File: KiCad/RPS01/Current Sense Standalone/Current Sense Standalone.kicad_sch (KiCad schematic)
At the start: 4 parts, among them U1 INA139QPWRQ1

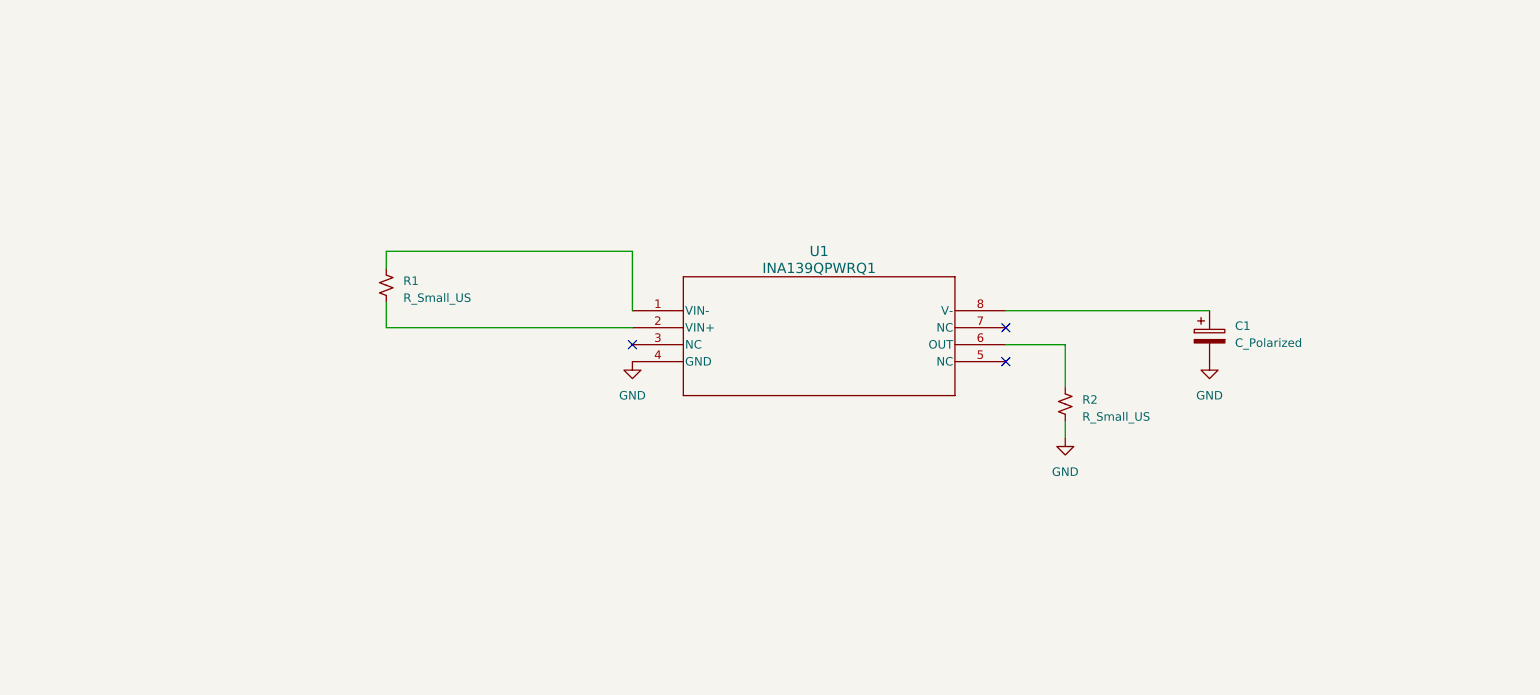
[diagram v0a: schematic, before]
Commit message: Current Sense
Updated schematic
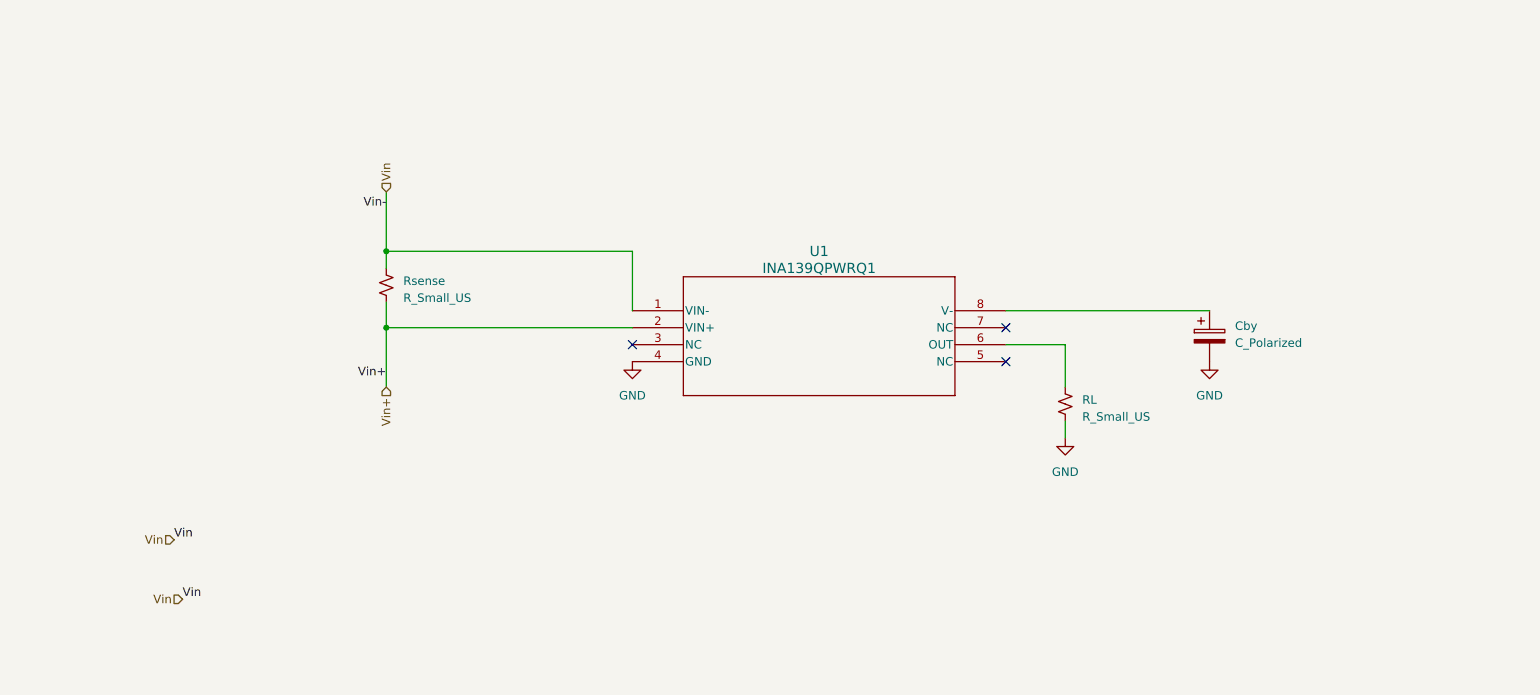
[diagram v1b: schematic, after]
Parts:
- renumbered C1 to Cby, R2 to RL, R1 to Rsense
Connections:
- net Vin: now reaches Rsense.1, U1.1 (VIN-)
- net Vin+: now reaches Rsense.2, U1.2 (VIN+)
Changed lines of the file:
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@@
 (kicad_sch (version 20230121) (generator eeschema)
   (paper "A4")
+  (junction (at 86.36 88.9) (diameter 0) (color 0 0 0 0)
+  )
+  (junction (at 86.36 100.33) (diameter 0) (color 0 0 0 0)
+  )
   (no_connect (at 123.19 102.87))
   (no_connect (at 179.07 100.33))
   (no_connect (at 179.07 105.41))
+  (wire (pts (xy 86.36 80.01) (xy 86.36 88.9))
+    (stroke (width 0) (type default))
+  )
+  (wire (pts (xy 86.36 100.33) (xy 86.36 109.22))
+    (stroke (width 0) (type default))
+  )
   (wire (pts (xy 86.36 88.9) (xy 86.36 91.44))
     (stroke (width 0) (type default))
@@
     (stroke (width 0) (type default))
   )
+  (label "Vin" (at 54.61 132.08 0) (fields_autoplaced)
+    (effects (font (size 1.27 1.27)) (justify left bottom))
+  )
+  (label "Vin+" (at 86.36 107.95 180) (fields_autoplaced)
+    (effects (font (size 1.27 1.27)) (justify right bottom))
+  )
+  (label "Vin" (at 55.88 140.97 0) (fields_autoplaced)
+    (effects (font (size 1.27 1.27)) (justify left bottom))
+  )
+  (label "Vin-" (at 86.36 82.55 180) (fields_autoplaced)
+    (effects (font (size 1.27 1.27)) (justify right bottom))
+  )
+  (hierarchical_label "Vin" (shape input) (at 55.88 140.97 180) (fields_autoplaced)
+    (effects (font (size 1.27 1.27)) (justify right))
+  )
+  (hierarchical_label "Vin" (shape input) (at 86.36 80.01 90) (fields_autoplaced)
+    (effects (font (size 1.27 1.27)) (justify left))
+  )
+  (hierarchical_label "Vin+" (shape input) (at 86.36 109.22 270) (fields_autoplaced)
+    (effects (font (size 1.27 1.27)) (justify right))
+  )
+  (hierarchical_label "Vin" (shape input) (at 54.61 132.08 180) (fields_autoplaced)
+    (effects (font (size 1.27 1.27)) (justify right))
+  )
   (symbol (lib_id "Device:R_Small_US") (at 187.96 111.76 0) (unit 1)
     (in_bom yes) (on_board yes) (dnp no) (fields_autoplaced)
-    (property "Reference" "R2" (at 190.5 111.125 0)
+    (property "Reference" "RL" (at 190.5 111.125 0)
       (effects (font (size 1.27 1.27)) (justify left))
     )
@@
       (project "Current Sense Standalone"
         (path "/af3dddb2-191c-40a1-9395-0fad50eefcf8"
-          (reference "R2") (unit 1)
+          (reference "RL") (unit 1)
         )
       )
@@
   (symbol (lib_id "Device:C_Polarized") (at 209.55 101.6 0) (unit 1)
     (in_bom yes) (on_board yes) (dnp no) (fields_autoplaced)
-    (property "Reference" "C1" (at 213.36 100.076 0)
+    (property "Reference" "Cby" (at 213.36 100.076 0)
       (effects (font (size 1.27 1.27)) (justify left))
     )
@@
       (project "Current Sense Standalone"
         (path "/af3dddb2-191c-40a1-9395-0fad50eefcf8"
-          (reference "C1") (unit 1)
+          (reference "Cby") (unit 1)
         )
       )
@@
   (symbol (lib_id "Device:R_Small_US") (at 86.36 93.98 0) (unit 1)
     (in_bom yes) (on_board yes) (dnp no) (fields_autoplaced)
-    (property "Reference" "R1" (at 88.9 93.345 0)
+    (property "Reference" "Rsense" (at 88.9 93.345 0)
       (effects (font (size 1.27 1.27)) (justify left))
     )
@@
       (project "Current Sense Standalone"
         (path "/af3dddb2-191c-40a1-9395-0fad50eefcf8"
-          (reference "R1") (unit 1)
-        )
-      )
+          (reference "Rsense") (unit 1)
+        )
+      )

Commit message: updated Current sense circuit
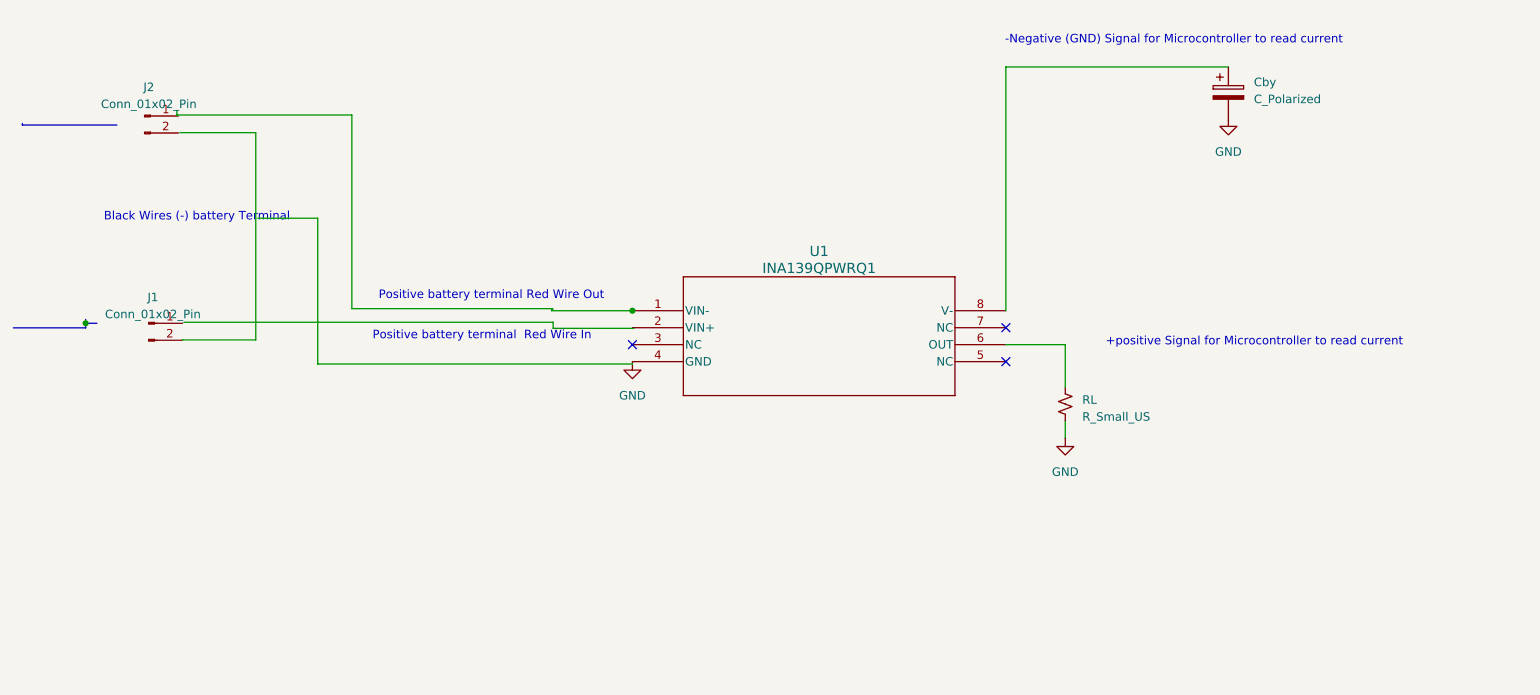
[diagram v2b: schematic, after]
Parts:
- removed Rsense: R_Small_US, Res_Bourns_CSS2H-3920R-L300F:Bourns-CSS2H-3920R-L300F-MFG, symbol Device:R_Small_US
- added J1, J2: Conn_01x02_Pin, symbol Connector:Conn_01x02_Pin
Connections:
- net Vin: no longer names the net of U1.1 (VIN-)
- net Vin+: no longer names the net of U1.2 (VIN+)
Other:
- note added: "+positive Signal for Microcontroller to read current"
- note added: "-Negative (GND) Signal for Microcontroller to read current"
- note added: "Black Wires (-) battery Terminal"
- note added: "Positive battery terminal Red Wire In"
- note added: "Positive battery terminal Red Wire Out"
- moved on the sheet: Cby

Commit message: Current Circuit setup.
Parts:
- removed J2: Conn_01x02_Pin, symbol Connector:Conn_01x02_Pin
- added J3: V+/- TEST Header PIN, symbol Connector:Conn_01x01_Pin
- added J4: BAT +TERMINAL TEST HEADER PIN, symbol Connector:Conn_01x01_Pin
- added J5: HEADER PIN FOR TEST, symbol Connector:Conn_01x01_Pin
- added J6: to MCU GPIO PIN, symbol Connector:Conn_01x01_Pin
- added J7: PLUG BATTERY OUTPUT HERE, symbol Connector:Conn_01x02_Pin
- J1: value Conn_01x02_Pin -> PLUG INPUT BATTERY IN HERE
